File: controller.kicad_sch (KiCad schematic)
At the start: 3 parts

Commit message: temp
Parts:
- JP2, JP3, JP4: value (none) -> 1x02_2.54; footprint (none) -> Connector_PinHeader_2.54mm:PinHeader_1x03_P2.54mm_Vertical; E14PART (none) -> 1593411; Element14 1593411 -> (none)

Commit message: Scary file corruption turns out to be just bugs in eschema.
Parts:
- JP2, JP3, JP4: value 1x02_2.54 -> (none); footprint Connector_PinHeader_2.54mm:PinHeader_1x03_P2.54mm_Vertical -> (none)

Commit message: Removed 'Element14' field from all sch/pcb components
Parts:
- JP2, JP3, JP4: value (none) -> 1x02_2.54; footprint (none) -> Connector_PinHeader_2.54mm:PinHeader_1x03_P2.54mm_Vertical
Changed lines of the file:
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@@
       (effects (font (size 1.27 1.27)) (justify right))
     )
-    (property "Value" "" (id 1) (at 165.735 54.61 0)
+    (property "Value" "1x02_2.54" (id 1) (at 165.735 54.61 0)
       (effects (font (size 1.27 1.27)) (justify right) hide)
     )
-    (property "Footprint" "" (id 2) (at 162.56 58.42 0)
+    (property "Footprint" "Connector_PinHeader_2.54mm:PinHeader_1x03_P2.54mm_Vertical" (id 2) (at 162.56 58.42 0)
       (effects (font (size 1.27 1.27)) hide)
     )
     (property "Datasheet" "~" (id 3) (at 162.56 58.42 0)
-      (effects (font (size 1.27 1.27)) hide)
-    )
-    (property "Element14" "" (id 4) (at 162.56 58.42 0)
       (effects (font (size 1.27 1.27)) hide)
     )
@@
       (effects (font (size 1.27 1.27)) (justify right))
     )
-    (property "Value" "" (id 1) (at 167.64 135.255 0)
+    (property "Value" "1x02_2.54" (id 1) (at 167.64 135.255 0)
       (effects (font (size 1.27 1.27)) (justify right) hide)
     )
-    (property "Footprint" "" (id 2) (at 163.83 132.08 0)
+    (property "Footprint" "Connector_PinHeader_2.54mm:PinHeader_1x03_P2.54mm_Vertical" (id 2) (at 163.83 132.08 0)
       (effects (font (size 1.27 1.27)) hide)
     )
     (property "Datasheet" "~" (id 3) (at 163.83 132.08 0)
-      (effects (font (size 1.27 1.27)) hide)
-    )
-    (property "Element14" "" (id 4) (at 163.83 132.08 0)
       (effects (font (size 1.27 1.27)) hide)
     )
@@
       (effects (font (size 1.27 1.27)) (justify right))
     )
-    (property "Value" "" (id 1) (at 160.02 150.495 0)
+    (property "Value" "1x02_2.54" (id 1) (at 160.02 150.495 0)
       (effects (font (size 1.27 1.27)) (justify right) hide)
     )
-    (property "Footprint" "" (id 2) (at 163.83 147.32 0)
+    (property "Footprint" "Connector_PinHeader_2.54mm:PinHeader_1x03_P2.54mm_Vertical" (id 2) (at 163.83 147.32 0)
       (effects (font (size 1.27 1.27)) hide)
     )
@@
       (effects (font (size 1.27 1.27)) hide)
     )
-    (property "Element14" "" (id 4) (at 163.83 147.32 0)
-      (effects (font (size 1.27 1.27)) hide)
-    )

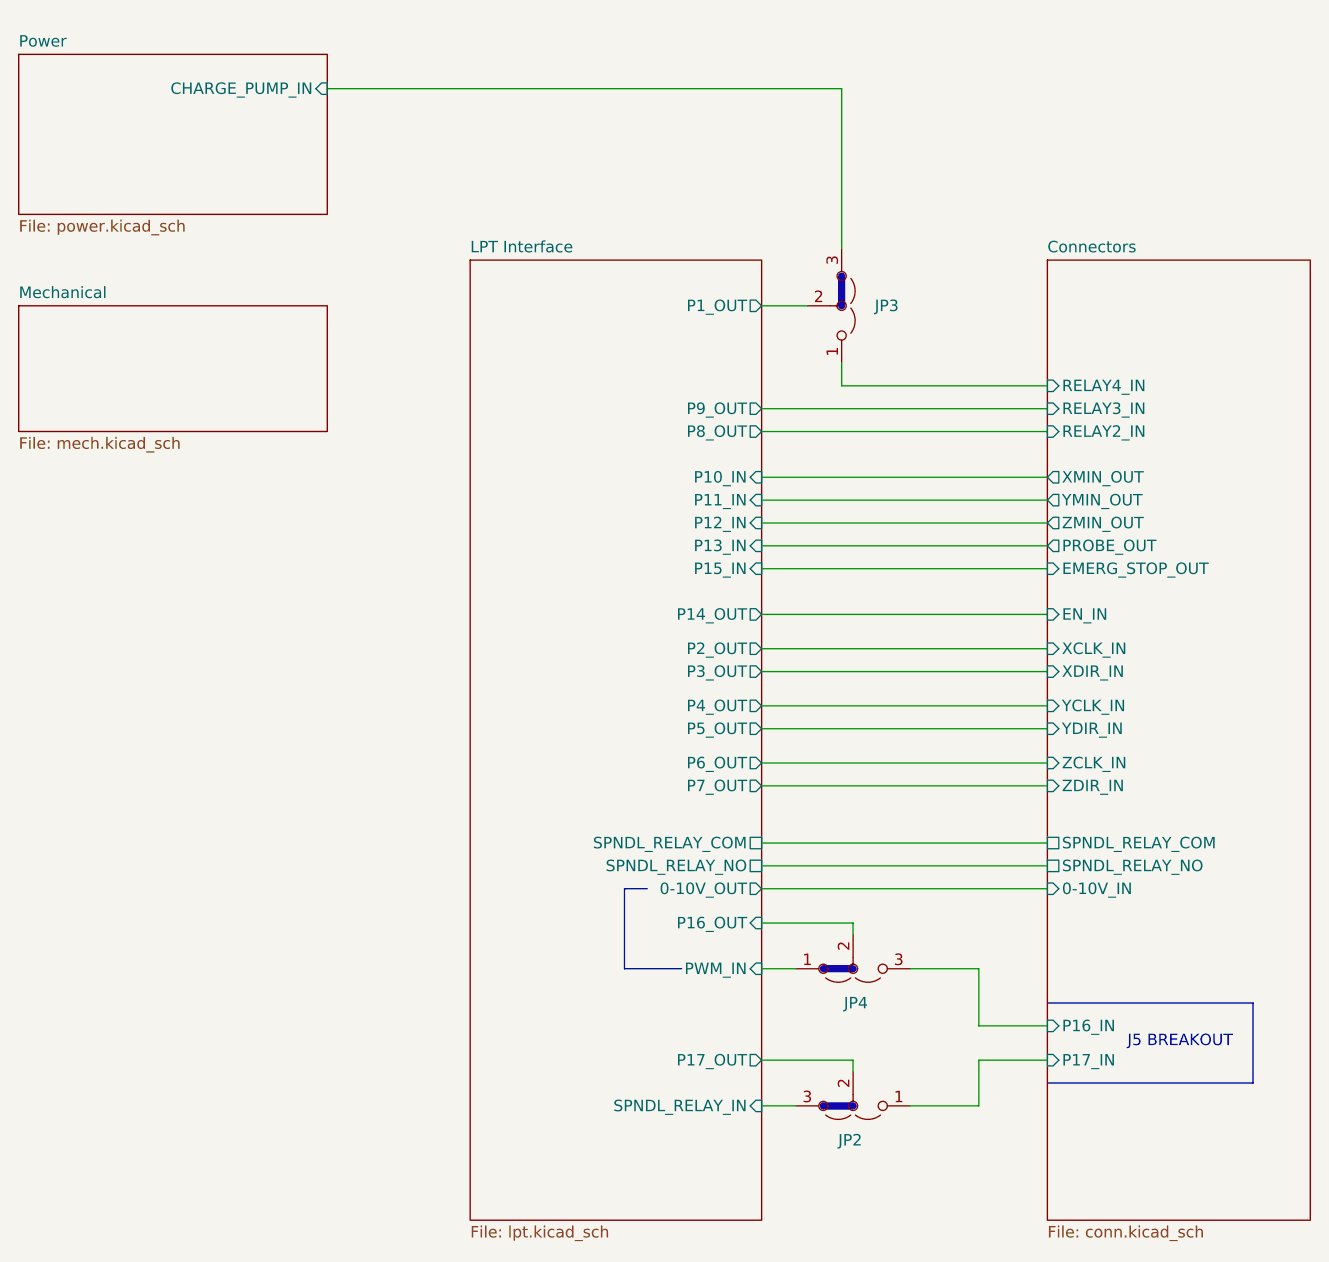
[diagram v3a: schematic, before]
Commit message: Reworked PSU control scheme (schematic only.)
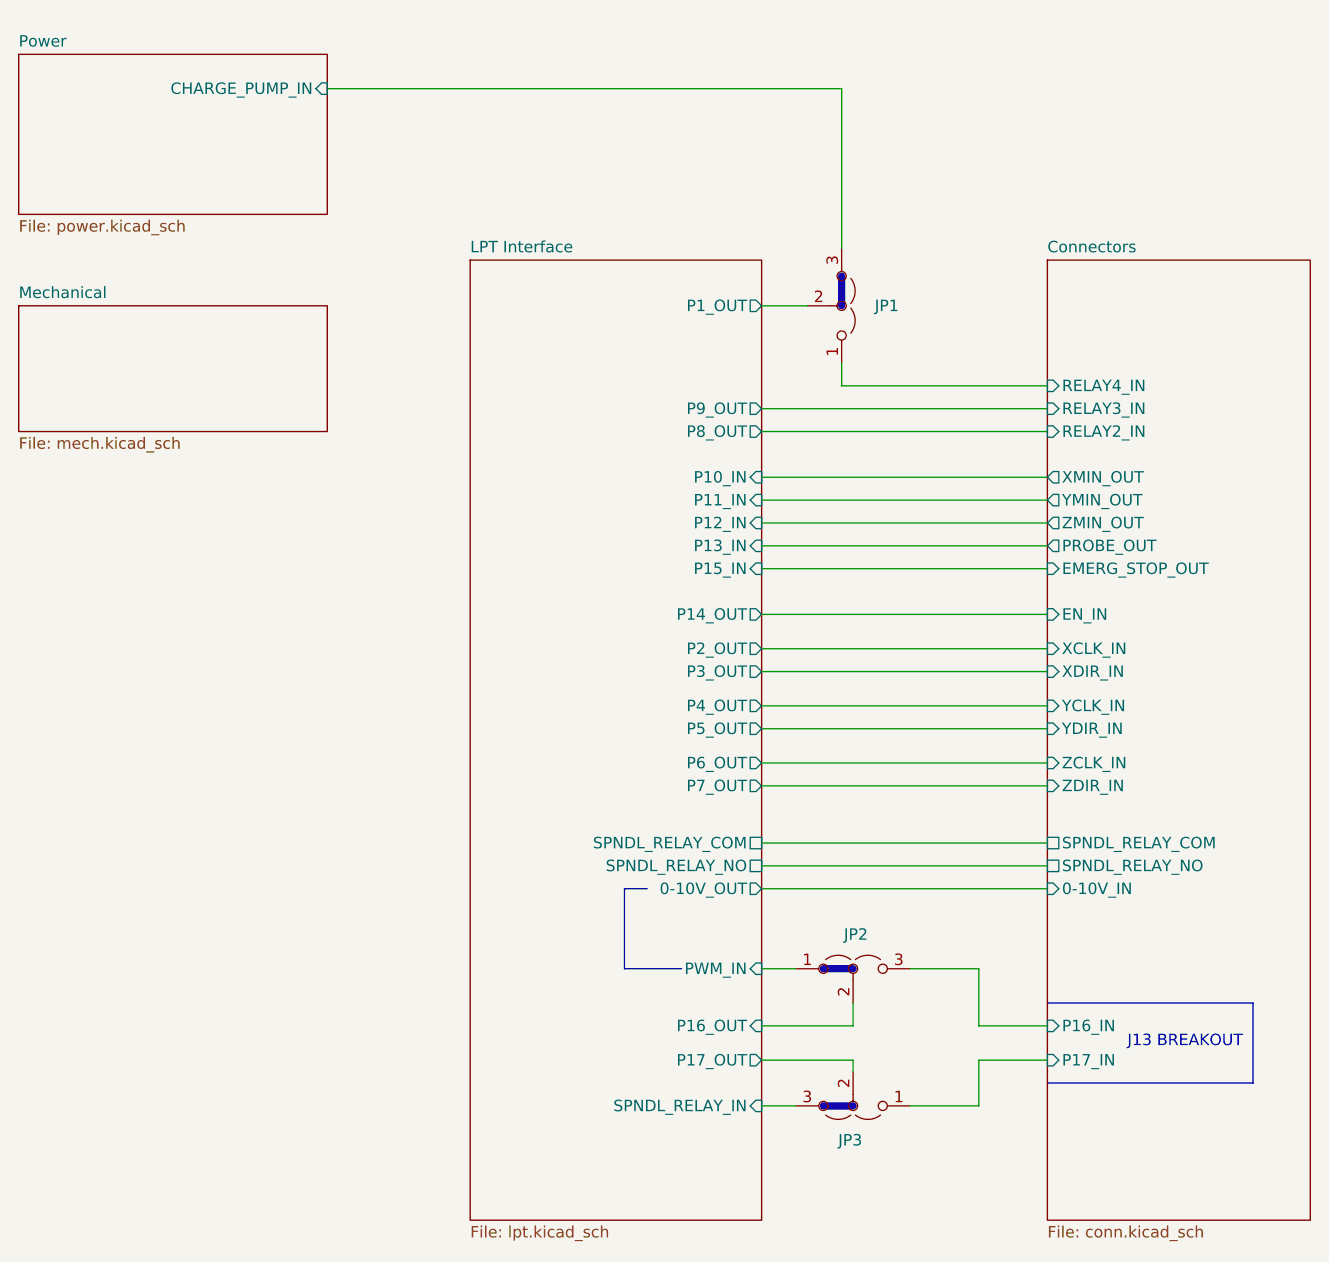
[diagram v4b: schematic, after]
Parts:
- renumbered JP3 to JP1, JP4 to JP2, JP2 to JP3
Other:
- note added: "J13 BREAKOUT"
- note removed: "J5 BREAKOUT"
- moved on the sheet: JP2

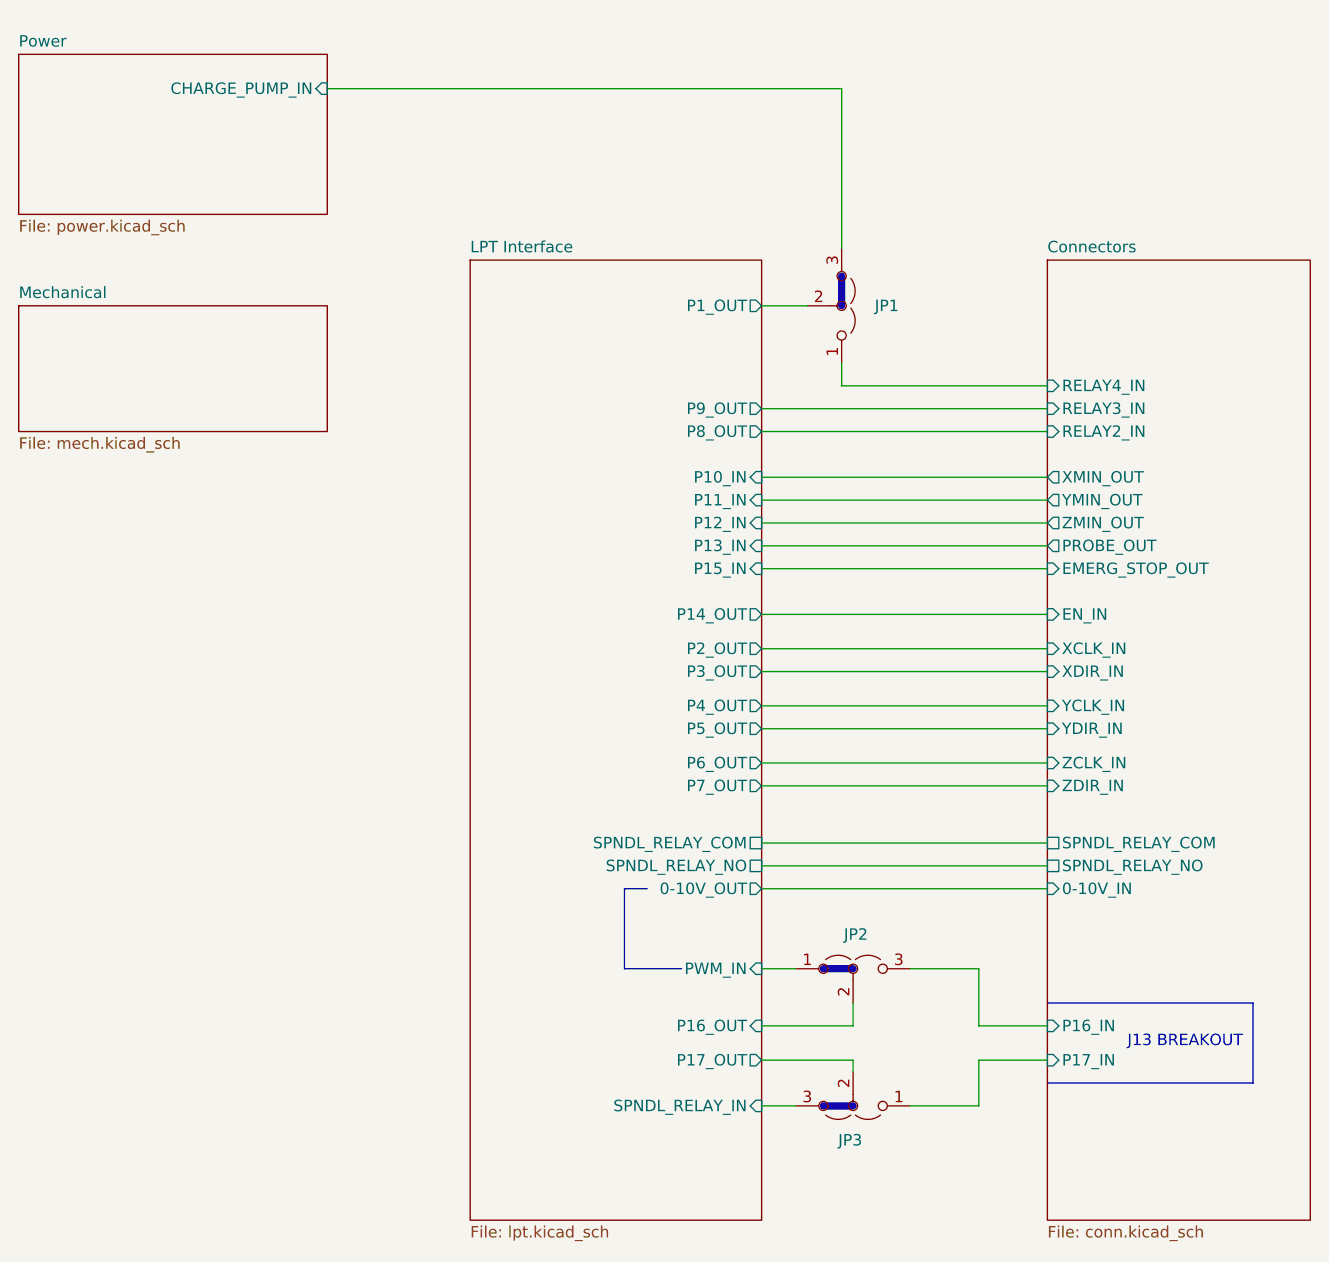
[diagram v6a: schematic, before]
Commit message: Routed power switching changes.
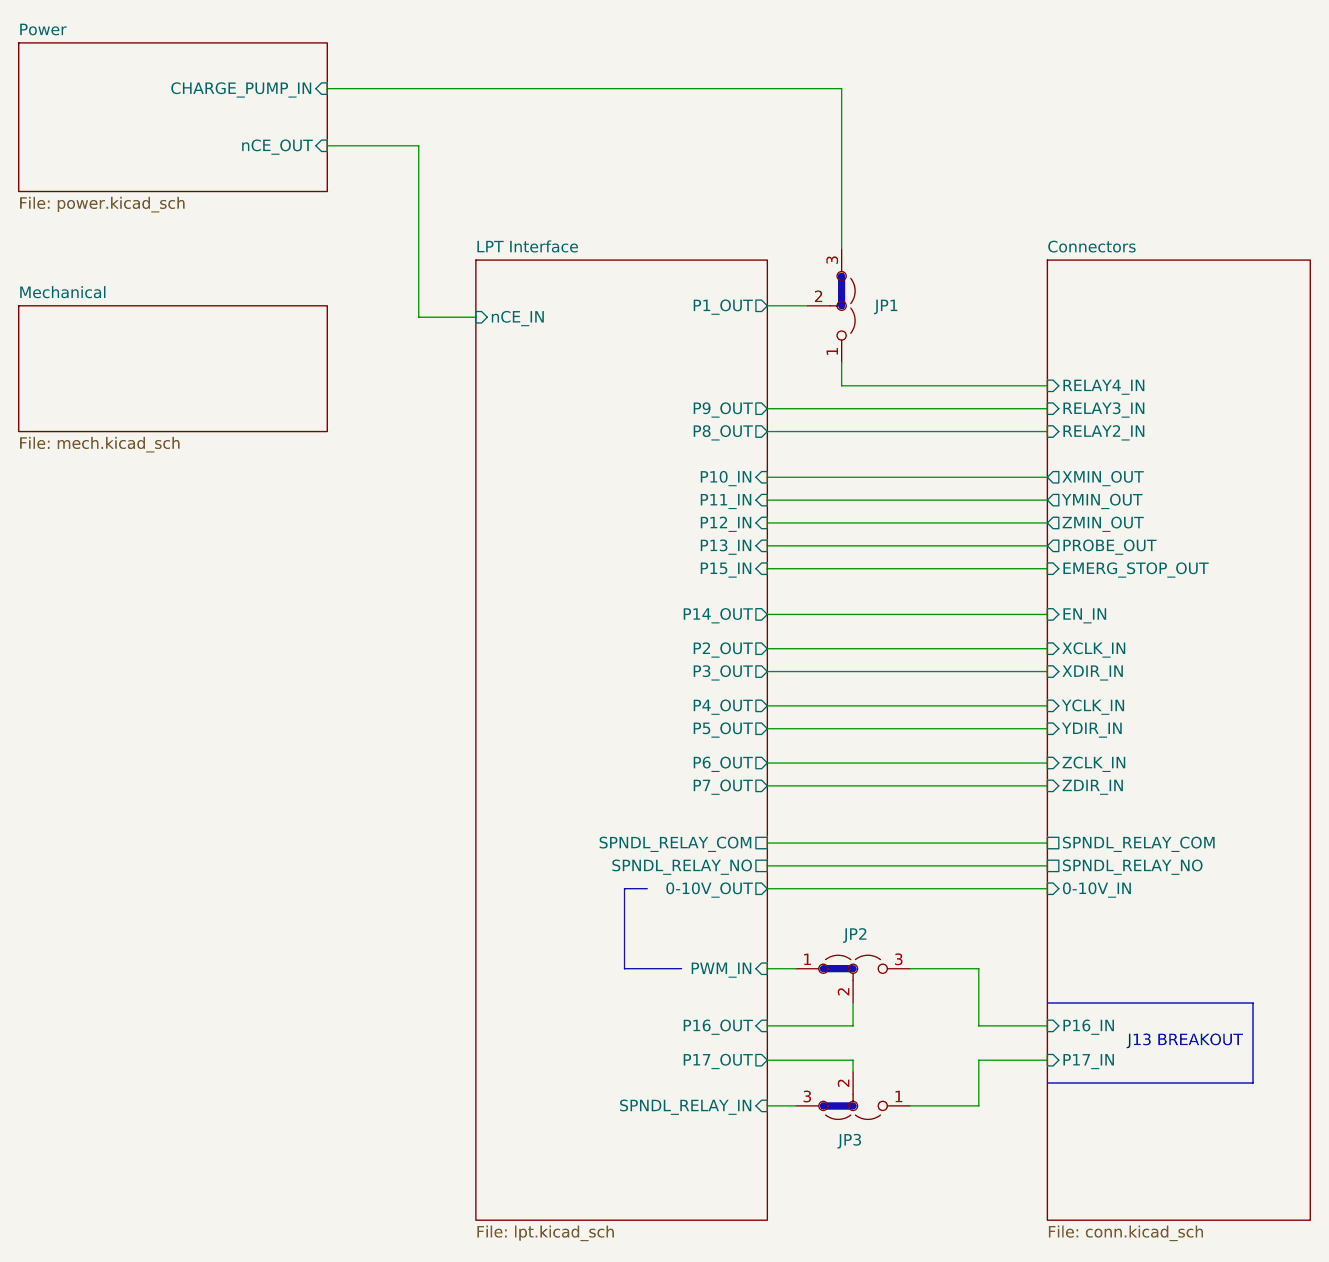
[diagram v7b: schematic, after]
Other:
- sheet LPT Interface ports: added nCE_IN; removed none
- sheet Power ports: added nCE_OUT; removed none
